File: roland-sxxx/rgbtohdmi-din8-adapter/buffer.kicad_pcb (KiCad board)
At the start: 2 copper layers, 69.8 x 23.1 mm, 9 parts, among them J1 DIN-8 Female (Symbol has 2 an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, P1 Conn_02x06_Odd_Even, P2 Conn_01x04, P6 Conn_01x01, P7 Conn_01x01, U1 74LS245

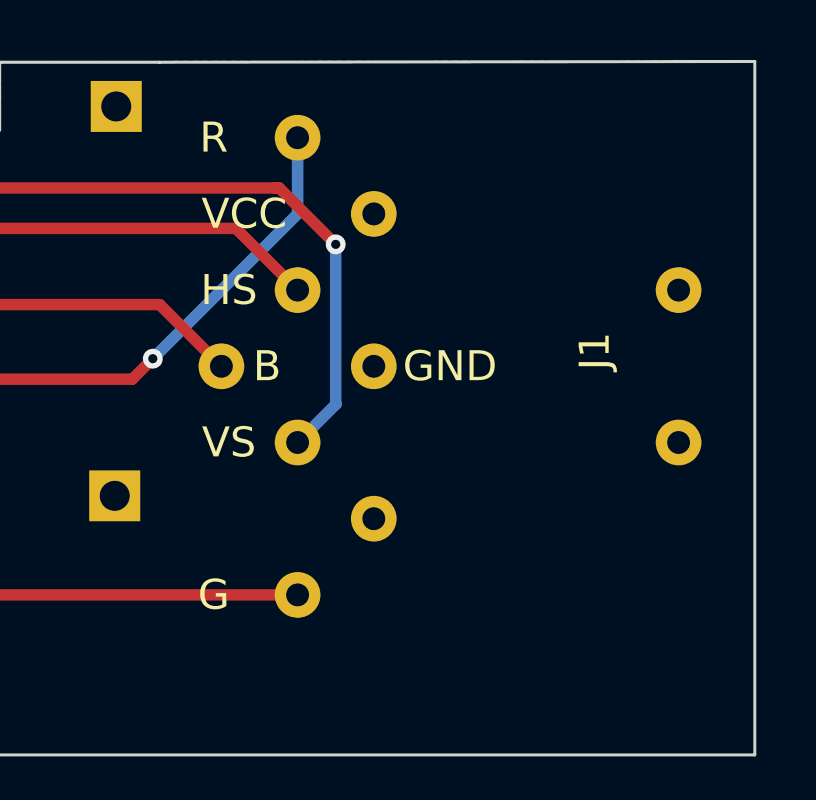
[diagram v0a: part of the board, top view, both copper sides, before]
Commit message: holes of the gerber were too small.
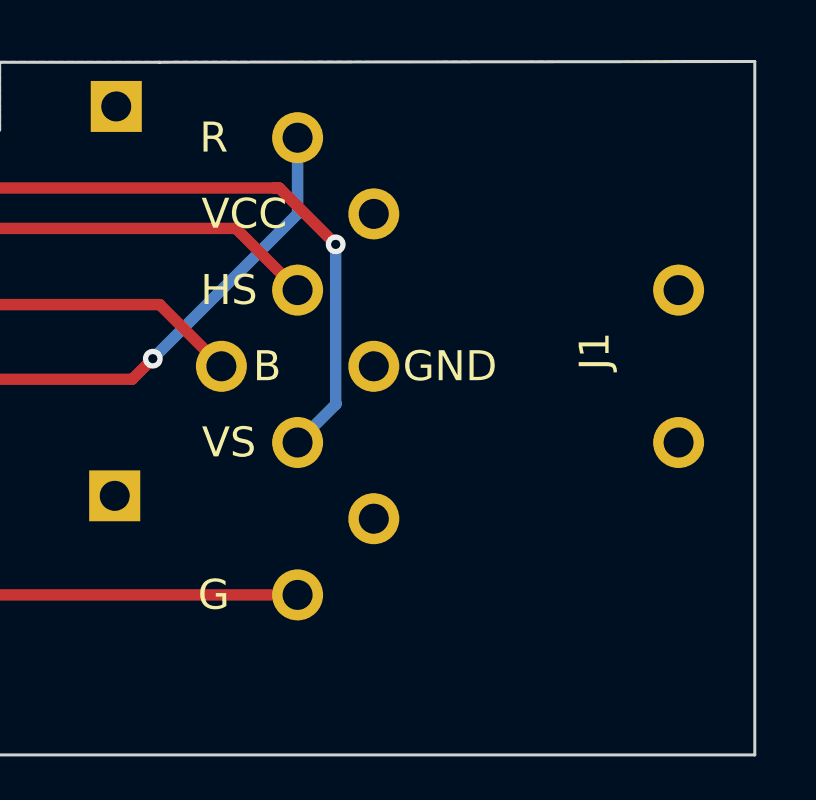
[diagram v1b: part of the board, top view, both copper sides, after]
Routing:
- net /I_B2: vias 1 -> 0
